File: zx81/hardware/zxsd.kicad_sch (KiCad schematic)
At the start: 37 parts, among them J1 Micro_SD_Card, J2 ZX81_EXP, SW1 RESET, U1 74HCT32, U10 27C256, U11 KM62256CLP, U2 74HCT32, U3 74HCT00, U4 74HCT02, U5 74HCT163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

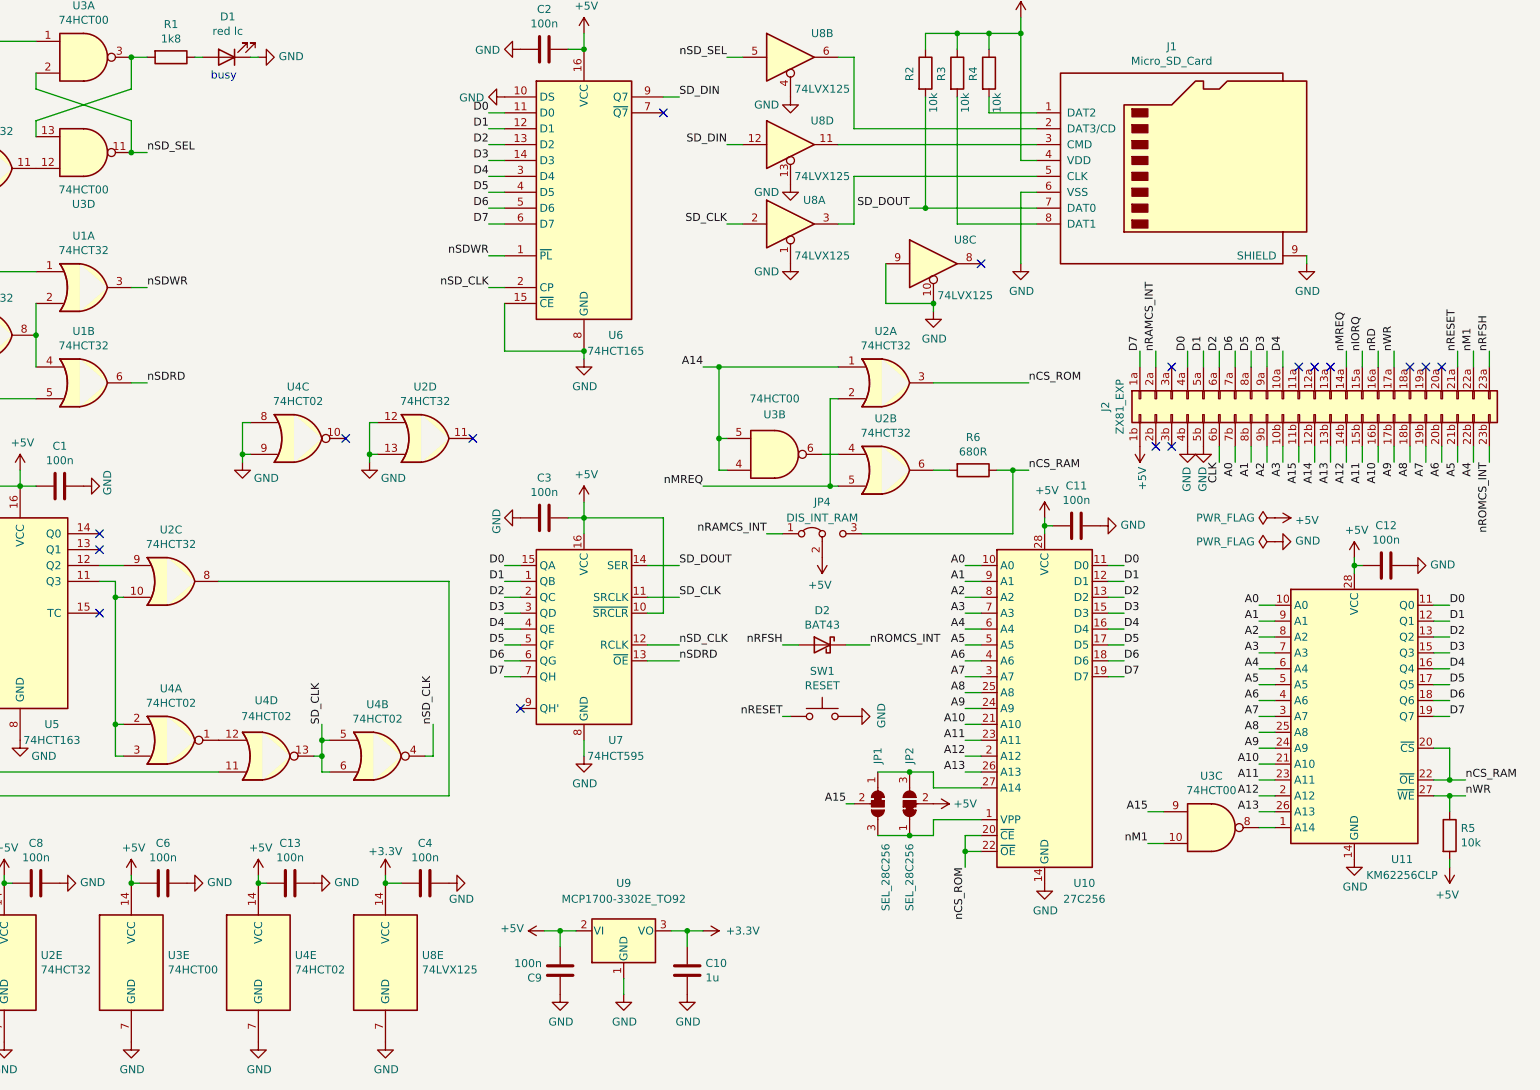
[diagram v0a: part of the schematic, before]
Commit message: fixed HRG issue, consider nRFSH for memory decoding
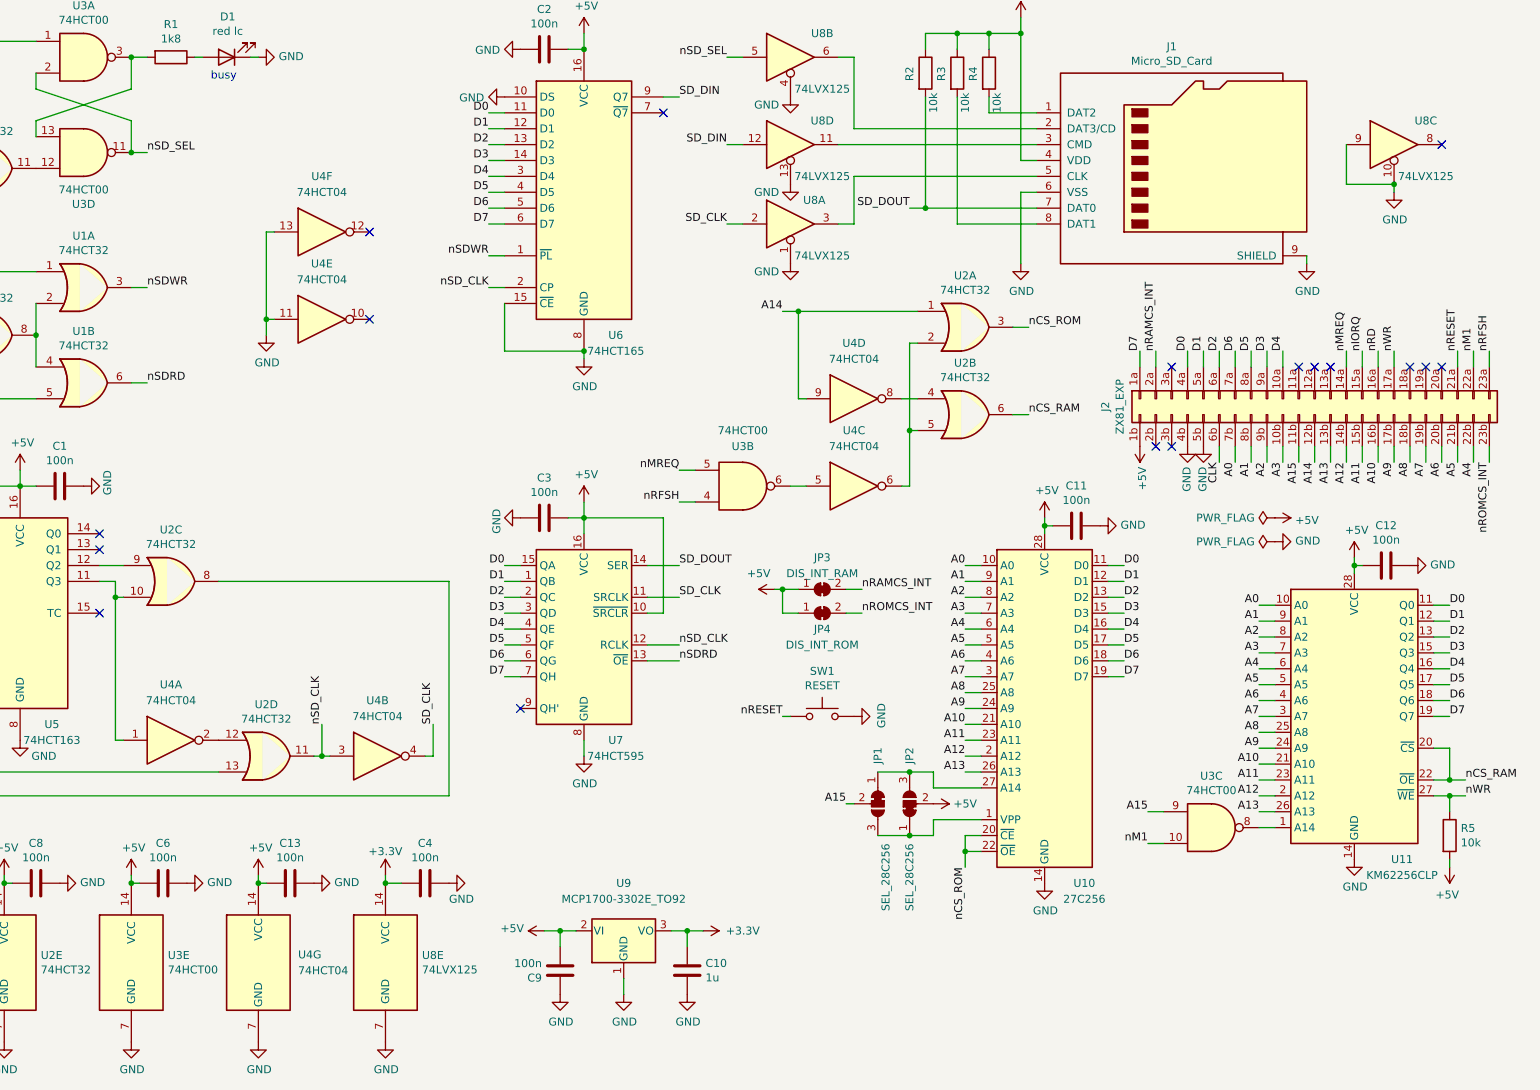
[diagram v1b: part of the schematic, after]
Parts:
- removed D2: BAT43, Diode_THT:D_DO-35_SOD27_P2.54mm_Vertical_AnodeUp, symbol Diode:BAT43
- removed JP4: DIS_INT_RAM, Connector_PinHeader_2.54mm:PinHeader_1x03_P2.54mm_Vertical, symbol Jumper:Jumper_3_Bridged12
- removed R6: 680R, Resistor_THT:R_Axial_DIN0207_L6.3mm_D2.5mm_P10.16mm_Horizontal, symbol Device:R
- removed U4: 74HCT02, Package_DIP:DIP-14_W7.62mm_Socket_LongPads, symbol 74xx:74LS02
- added JP3: DIS_INT_RAM, Jumper:SolderJumper-2_P1.3mm_Bridged_RoundedPad1.0x1.5mm, symbol Jumper:SolderJumper_2_Bridged
- added JP4: DIS_INT_ROM, Jumper:SolderJumper-2_P1.3mm_Bridged_RoundedPad1.0x1.5mm, symbol Jumper:SolderJumper_2_Bridged
- added U4: 74HCT04, Package_DIP:DIP-14_W7.62mm_Socket_LongPads, symbol 74xx:74LS04
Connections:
- net +5V: now also JP3.1 (A), JP4.1 (A), U4.14 (VCC)
- net A14: now also U4.9; no longer U3.4, U3.5
- net CLK: now also U2.13
- net GND: now also U4.11, U4.13, U4.7 (GND); no longer U2.12, U2.13
- net SD_CLK: now also U4.4
- net nCS_RAM: now also U2.6
- net nMREQ: now also U3.5; no longer U2.2, U2.5
- net nRAMCS_INT: now also JP3.2 (B)
- net nRFSH: now also U3.4
- net nROMCS_INT: now also JP4.2 (B)
- net nSD_CLK: now also U2.11, U4.3
- net at U2.10, U5.11 (Q3): now also U4.1
- net at U3.6: now also U4.5; no longer U2.4
- new net: U2.2, U2.5, U4.6
- new net: U2.4, U4.8
- new net: U2.12, U4.2
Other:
- moved on the sheet: U2A, U2B, U2D, U3B, U8C

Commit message: optimized RAM OE generation (thanks to Sigi)
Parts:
- removed R5: 10k, Resistor_THT:R_Axial_DIN0207_L6.3mm_D2.5mm_P10.16mm_Horizontal, symbol Device:R
- added D2, D3: BAT43, Diode_THT:D_DO-35_SOD27_P7.62mm_Horizontal, symbol Diode:BAT43
- added R6: 4k7, Resistor_THT:R_Axial_DIN0207_L6.3mm_D2.5mm_P10.16mm_Horizontal, symbol Device:R
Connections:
- net +5V: now also R6.1
- net nCS_RAM: no longer U11.22 (~{OE})
- net nRD: now also D2.1 (K)
- net nRFSH: now also D3.1 (K)
- new net nOE_RAM: D2.2 (A), D3.2 (A), R6.2, U11.22 (~{OE})

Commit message: some cosmetical fixes
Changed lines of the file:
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@@
     (stroke (width 0) (type default) (color 0 0 0 0))
   )
-  (wire (pts (xy 270.51 143.51) (xy 275.59 143.51))
+  (wire (pts (xy 270.51 143.51) (xy 273.05 143.51))
     (stroke (width 0) (type default) (color 0 0 0 0))
   )
@@
     (stroke (width 0) (type default) (color 0 0 0 0))
   )
-  (wire (pts (xy 270.51 140.97) (xy 275.59 140.97))
+  (wire (pts (xy 270.51 140.97) (xy 273.05 140.97))
     (stroke (width 0) (type default) (color 0 0 0 0))
   )
@@
     (stroke (width 0) (type default) (color 0 0 0 0))
   )
-  (wire (pts (xy 270.51 135.89) (xy 275.59 135.89))
+  (wire (pts (xy 270.51 135.89) (xy 273.05 135.89))
     (stroke (width 0) (type default) (color 0 0 0 0))
   )
@@
     (effects (font (size 1.27 1.27)) (justify left bottom))
   )
-  (label "nOE_RAM" (at 275.59 140.97 0)
+  (label "nOE_RAM" (at 273.05 140.97 0)
     (effects (font (size 1.27 1.27)) (justify left bottom))
   )
@@
     (effects (font (size 1.27 1.27)) (justify left bottom))
   )
-  (label "nWR" (at 275.59 143.51 0)
+  (label "nWR" (at 273.05 143.51 0)
     (effects (font (size 1.27 1.27)) (justify left bottom))
   )
@@
     (effects (font (size 1.27 1.27)) (justify right bottom))
   )
-  (label "nCS_RAM" (at 275.59 135.89 0)
+  (label "nCS_RAM" (at 273.05 135.89 0)
     (effects (font (size 1.27 1.27)) (justify left bottom))
   )
@@
   (symbol (lib_id "74xx:74LS00") (at 234.95 148.59 0) (unit 3)
     (in_bom yes) (on_board yes)
-    (property "Reference" "U3" (id 0) (at 234.95 140.335 0))
-    (property "Value" "74HCT00" (id 1) (at 234.95 142.6464 0))
+    (property "Reference" "U3" (id 0) (at 233.68 139.7 0))
+    (property "Value" "74HCT00" (id 1) (at 233.68 142.24 0))
     (property "Footprint" "Package_DIP:DIP-14_W7.62mm_Socket_LongPads" (id 2) (at 234.95 148.59 0)
       (effects (font (size 1.27 1.27)) hide)

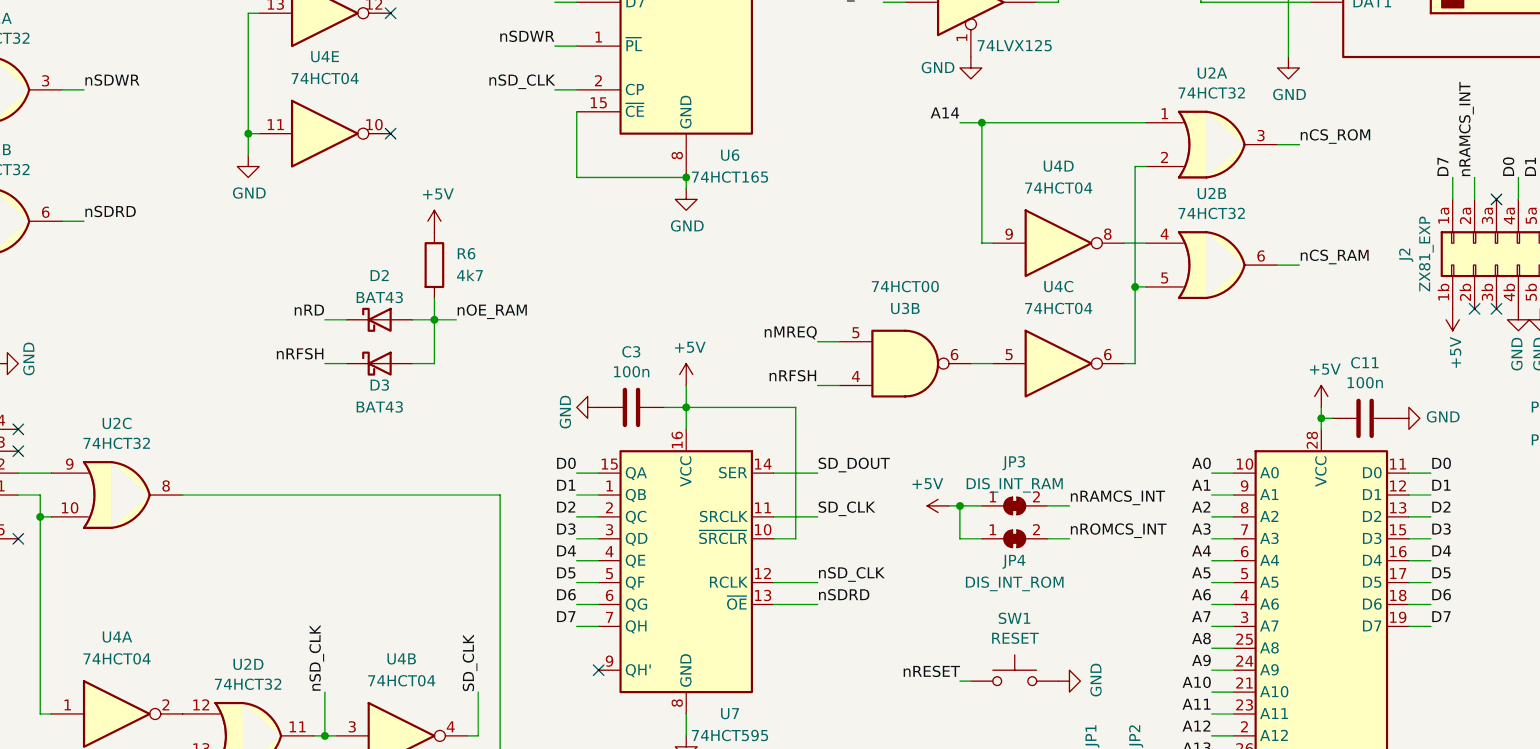
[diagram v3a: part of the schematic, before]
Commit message: re-fixed external ROM/EEPROM timing issue
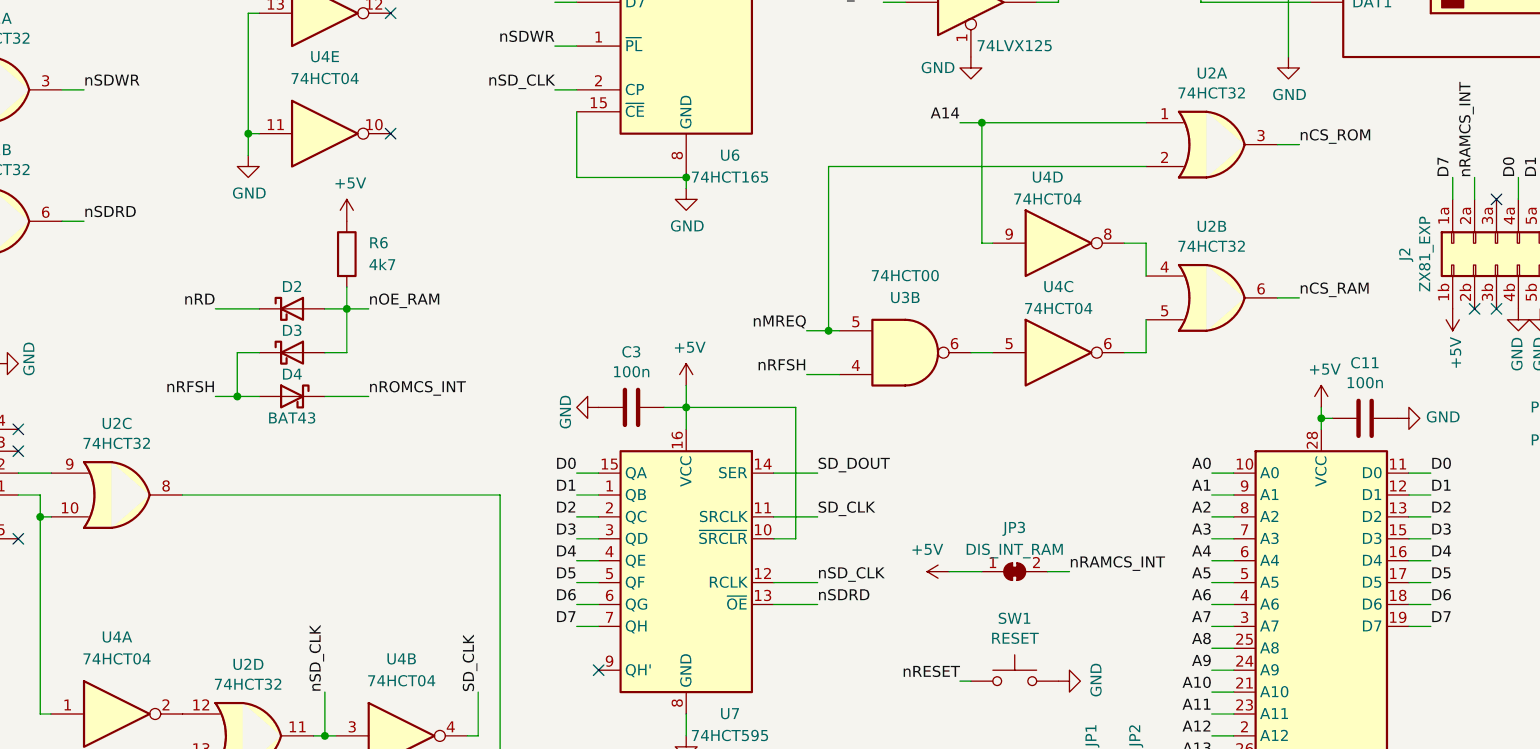
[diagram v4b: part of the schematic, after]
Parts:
- removed JP4: DIS_INT_ROM, Jumper:SolderJumper-2_P1.3mm_Bridged_RoundedPad1.0x1.5mm, symbol Jumper:SolderJumper_2_Bridged
- added D4: BAT43, Diode_THT:D_DO-35_SOD27_P2.54mm_Vertical_AnodeUp, symbol Diode:BAT43
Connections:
- net nMREQ: now also U2.2
- net nRFSH: now also D4.2 (A)
- net nROMCS_INT: now also D4.1 (K)
- net at U2.5, U4.6: no longer U2.2
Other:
- moved on the sheet: D2, D3, JP3, R6, U2B, U3B, U4C

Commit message: first full decoding for RAM and int+ext ROM
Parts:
- removed D2, D3: BAT43, Diode_THT:D_DO-35_SOD27_P7.62mm_Horizontal, symbol Diode:BAT43
- removed D4: BAT43, Diode_THT:D_DO-35_SOD27_P2.54mm_Vertical_AnodeUp, symbol Diode:BAT43
- removed R6: 4k7, Resistor_THT:R_Axial_DIN0207_L6.3mm_D2.5mm_P10.16mm_Horizontal, symbol Device:R
- added U12: 74HCT32, Package_DIP:DIP-14_W7.62mm_Socket_LongPads, symbol 74xx:74LS32
- added U13: 74HCT08, Package_DIP:DIP-14_W7.62mm_Socket_LongPads, symbol 74xx:74LS08
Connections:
- net A14: now also U12.4, U12.9; no longer U2.1
- net A15: now also U13.9; no longer U3.9
- net nCS_RAM: now also U12.3; no longer U2.6
- net nCS_ROM: now also U12.8; no longer U2.3
- net nM1: now also U13.10; no longer U3.10
- net nMREQ: now also U12.13, U13.4; no longer U2.2, U3.5
- net nOE_RAM: now also U13.3
- net nRD: now also U13.2
- net nRFSH: now also U4.5, U12.5, U13.1, U13.5; no longer U3.4
- net nROMCS_INT: now also U12.6
- net at U11.1 (A14): now also U13.8; no longer U3.8
- net at U3.6: no longer U4.5
- net at U2.4: no longer U4.8
- net at U2.5: no longer U4.6
- new net: U12.10, U12.11
- new net: U12.12, U4.6
- new net: U12.1, U4.8
- new net: U12.2, U13.6
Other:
- moved on the sheet: U2A, U2B, U3B, U3C, U4C, U4D, U4E, U4F

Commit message: optimized RAM/ROM decoder logic
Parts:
- removed U12: 74HCT32, Package_DIP:DIP-14_W7.62mm_Socket_LongPads, symbol 74xx:74LS32
- added C5: 100n, Capacitor_THT:C_Disc_D5.0mm_W2.5mm_P5.00mm, symbol Device:C
- renumbered U13 to U12
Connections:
- net +5V: now also U12.14 (VCC), C5.1
- net A14: now also U2.1, U2.4, U3.5; no longer U4.9
- net GND: now also U12.12, U12.13, U12.7 (GND), C5.2
- net nCS_RAM: now also U3.6
- net nCS_ROM: now also U2.6
- net nMREQ: now also U4.9
- net nRFSH: now also U2.2, U3.9; no longer U4.5
- net nROMCS_INT: now also U2.3
- net at U3.10: now also U4.8
- net at U3.8: now also U2.5
- net at U3.4: now also U4.6
- net at U12.6: now also U4.5
- no-connect marks 17 -> 18
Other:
- moved on the sheet: C10, C3, C4, C9, D1, R1, U12A, U12B, U12D, U12E, U1A, U1B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
